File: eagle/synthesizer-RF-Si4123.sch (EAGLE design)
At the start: 46 parts, among them J1 142-0701-851, J2 142-0701-851, J3 142-0701-851, U1 LP38692, U2 SI4123, X1 ECS-TXO-3225

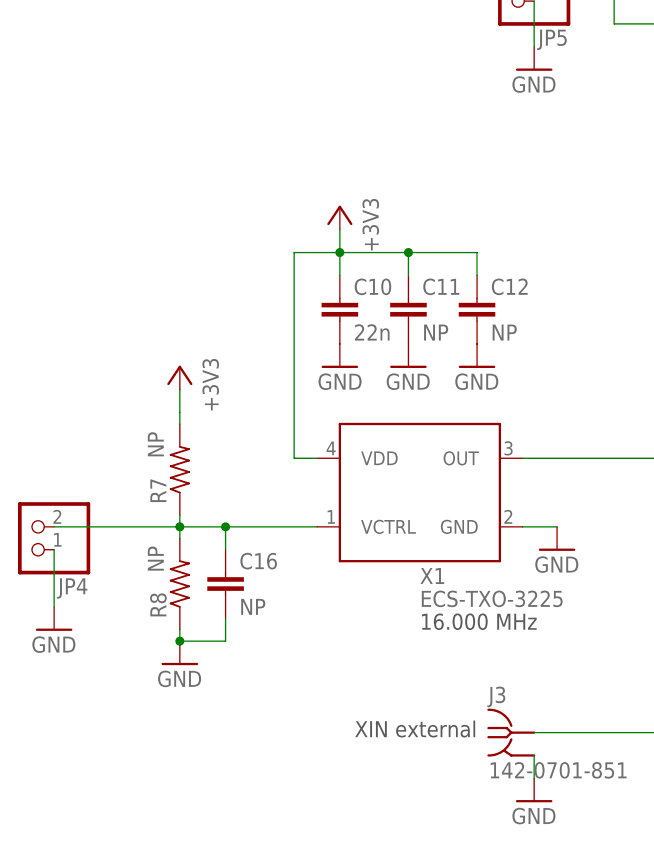
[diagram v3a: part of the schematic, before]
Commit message: Add 0ohm to TCXO, & minor tweaks.
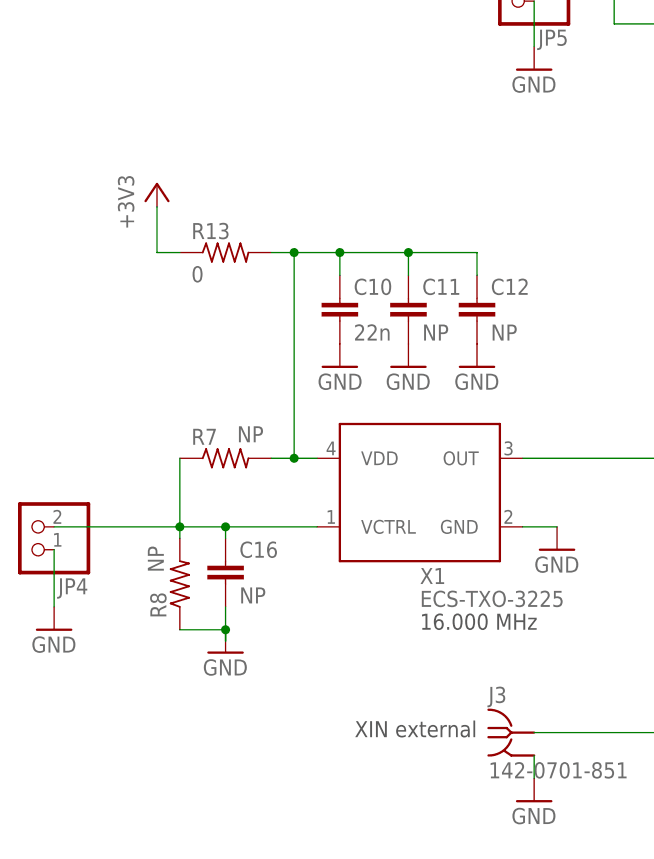
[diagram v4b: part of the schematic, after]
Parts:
- added R13: 0, oresat-rcl:R-US_0805-B-NOSILK
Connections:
- new net N$10: C10.1, C11.1, C12.1, R13.2, R7.2, X1.VDD
- net +3V3: now also R13.1; no longer C10.1, C11.1, C12.1, R7.2, X1.VDD
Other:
- moved on the sheet: C16, R7
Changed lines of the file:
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@@
 <part name="R7" library="oresat-rcl" deviceset="R-US_" device="0603-B-NOSILK" value="NP"/>
 <part name="R8" library="oresat-rcl" deviceset="R-US_" device="0603-B-NOSILK" value="NP"/>
-<part name="+3V1" library="supply1" library_urn="urn:adsk.eagle:library:371" deviceset="+3V3" device=""/>
 <part name="GND10" library="supply1" library_urn="urn:adsk.eagle:library:371" deviceset="GND" device=""/>
 <part name="GND11" library="supply1" library_urn="urn:adsk.eagle:library:371" deviceset="GND" device=""/>
@@
 <part name="L2" library="oresat-rcl" deviceset="L-US" device="0402-C-NOSILK" value="18/2.7n"/>
 <part name="L3" library="oresat-rcl" deviceset="L-US" device="0402-B-NOSILK" value="2n"/>
+<part name="R13" library="oresat-rcl" deviceset="R-US_" device="0805-B-NOSILK" value="0"/>
 </parts>
 <sheets>
@@
 <attribute name="VALUE" x="101.6" y="125.73" size="1.778" layer="96" rot="R90"/>
 </instance>
-<instance part="+3V8" gate="G$1" x="55.88" y="81.28" smashed="yes" rot="MR0">
-<attribute name="VALUE" x="58.42" y="76.2" size="1.778" layer="96" rot="MR90"/>
+<instance part="+3V8" gate="G$1" x="35.56" y="83.82" smashed="yes">
+<attribute name="VALUE" x="33.02" y="78.74" size="1.778" layer="96" rot="R90"/>
 </instance>
 <instance part="JP4" gate="G$1" x="21.59" y="45.72" smashed="yes" rot="R180">
@@
 </instance>
 <instance part="JMP1" gate="G$2" x="106.68" y="50.8" smashed="yes"/>
-<instance part="R7" gate="R" x="38.1" y="52.07" smashed="yes" rot="R90">
-<attribute name="NAME" x="36.6014" y="48.26" size="1.778" layer="95" rot="R90"/>
-<attribute name="VALUE" x="36.322" y="53.34" size="1.778" layer="96" rot="R90"/>
+<instance part="R7" gate="R" x="43.18" y="53.34" smashed="yes">
+<attribute name="NAME" x="39.37" y="54.8386" size="1.778" layer="95"/>
+<attribute name="VALUE" x="44.45" y="55.118" size="1.778" layer="96"/>
 </instance>
 <instance part="R8" gate="R" x="38.1" y="39.37" smashed="yes" rot="R90">
@@
 <attribute name="VALUE" x="36.322" y="40.64" size="1.778" layer="96" rot="R90"/>
 </instance>
-<instance part="+3V1" gate="G$1" x="38.1" y="63.5" smashed="yes" rot="MR0">
-<attribute name="VALUE" x="40.64" y="58.42" size="1.778" layer="96" rot="MR90"/>
-</instance>
-<instance part="GND10" gate="1" x="38.1" y="30.48" smashed="yes">
-<attribute name="VALUE" x="35.56" y="27.94" size="1.778" layer="96"/>
+<instance part="GND10" gate="1" x="43.18" y="31.75" smashed="yes">
+<attribute name="VALUE" x="40.64" y="29.21" size="1.778" layer="96"/>
 </instance>
 <instance part="GND11" gate="1" x="91.44" y="166.37" smashed="yes">
@@
 <attribute name="VALUE" x="186.182" y="66.04" size="1.778" layer="96" rot="R90"/>
 </instance>
-<instance part="C16" gate="CE" x="43.18" y="40.64" smashed="yes">
-<attribute name="NAME" x="44.704" y="41.021" size="1.778" layer="95"/>
-<attribute name="VALUE" x="44.704" y="35.941" size="1.778" layer="96"/>
+<instance part="C16" gate="CE" x="43.18" y="41.91" smashed="yes">
+<attribute name="NAME" x="44.704" y="42.291" size="1.778" layer="95"/>
+<attribute name="VALUE" x="44.704" y="37.211" size="1.778" layer="96"/>
 </instance>
 <instance part="L1" gate="L" x="119.38" y="95.25" smashed="yes" rot="R90">
@@
 <attribute name="NAME" x="185.42" y="102.87" size="1.778" layer="95" rot="R180"/>
 <attribute name="VALUE" x="180.34" y="102.87" size="1.778" layer="96" rot="R180"/>
+</instance>
+<instance part="R13" gate="R" x="43.18" y="76.2" smashed="yes">
+<attribute name="NAME" x="39.37" y="77.6986" size="1.778" layer="95"/>
+<attribute name="VALUE" x="39.37" y="72.898" size="1.778" layer="96"/>
 </instance>
 </instances>
@@
 <pinref part="R8" gate="R" pin="1"/>
 <pinref part="GND10" gate="1" pin="GND"/>
-<wire x1="38.1" y1="34.29" x2="38.1" y2="33.02" width="0.1524" layer="91"/>
+<wire x1="38.1" y1="34.29" x2="43.18" y2="34.29" width="0.1524" layer="91"/>
 <pinref part="C16" gate="CE" pin="2"/>
-<wire x1="38.1" y1="33.02" x2="43.18" y2="33.02" width="0.1524" layer="91"/>
-<wire x1="43.18" y1="33.02" x2="43.18" y2="35.56" width="0.1524" layer="91"/>
-<junction x="38.1" y="33.02"/>
+<wire x1="43.18" y1="34.29" x2="43.18" y2="33.02" width="0.1524" layer="91"/>
+<wire x1="43.18" y1="33.02" x2="43.18" y2="36.83" width="0.1524" layer="91"/>
+<junction x="43.18" y="34.29"/>
 </segment>
 <segment>
@@
 <wire x1="104.14" y1="125.73" x2="104.14" y2="128.27" width="0.1524" layer="91"/>
 <pinref part="+3V7" gate="G$1" pin="+3V3"/>
-</segment>
-<segment>
-<pinref part="C12" gate="CE" pin="1"/>
-<wire x1="71.12" y1="73.66" x2="71.12" y2="76.2" width="0.1524" layer="91"/>
-<pinref part="C11" gate="CE" pin="1"/>
-<wire x1="63.5" y1="73.66" x2="63.5" y2="76.2" width="0.1524" layer="91"/>
-<wire x1="63.5" y1="76.2" x2="71.12" y2="76.2" width="0.1524" layer="91"/>
-<pinref part="C10" gate="CE" pin="1"/>
-<wire x1="63.5" y1="76.2" x2="55.88" y2="76.2" width="0.1524" layer="91"/>
-<wire x1="55.88" y1="76.2" x2="55.88" y2="73.66" width="0.1524" layer="91"/>
-<junction x="63.5" y="76.2"/>
-<junction x="55.88" y="76.2"/>
-<wire x1="55.88" y1="78.74" x2="55.88" y2="76.2" width="0.1524" layer="91"/>
-<pinref part="+3V8" gate="G$1" pin="+3V3"/>
-<pinref part="X1" gate="G$1" pin="VDD"/>
-<wire x1="53.34" y1="53.34" x2="50.8" y2="53.34" width="0.1524" layer="91"/>
-<wire x1="50.8" y1="53.34" x2="50.8" y2="76.2" width="0.1524" layer="91"/>
-<wire x1="50.8" y1="76.2" x2="55.88" y2="76.2" width="0.1524" layer="91"/>
-</segment>
-<segment>
-<pinref part="R7" gate="R" pin="2"/>
-<pinref part="+3V1" gate="G$1" pin="+3V3"/>
-<wire x1="38.1" y1="57.15" x2="38.1" y2="58.42" width="0.1524" layer="91"/>
-<wire x1="38.1" y1="58.42" x2="38.1" y2="60.96" width="0.1524" layer="91"/>
 </segment>
 <segment>
@@
 <wire x1="149.86" y1="185.42" x2="111.76" y2="185.42" width="0.1524" layer="91"/>
 </segment>
+<segment>
+<pinref part="+3V8" gate="G$1" pin="+3V3"/>
+<pinref part="R13" gate="R" pin="1"/>
+<wire x1="35.56" y1="81.28" x2="35.56" y2="76.2" width="0.1524" layer="91"/>
+<wire x1="35.56" y1="76.2" x2="38.1" y2="76.2" width="0.1524" layer="91"/>
+</segment>
 </net>
 <net name="N$19" class="0">
@@
 <wire x1="43.18" y1="45.72" x2="38.1" y2="45.72" width="0.1524" layer="91"/>
 <wire x1="38.1" y1="45.72" x2="24.13" y2="45.72" width="0.1524" layer="91"/>
-<wire x1="38.1" y1="46.99" x2="38.1" y2="45.72" width="0.1524" layer="91"/>
+<wire x1="38.1" y1="53.34" x2="38.1" y2="45.72" width="0.1524" layer="91"/>
 <junction x="38.1" y="45.72"/>
 <pinref part="R8" gate="R" pin="2"/>
@@
 <junction x="43.18" y="45.72"/>
 <pinref part="C16" gate="CE" pin="1"/>
-<wire x1="43.18" y1="43.18" x2="43.18" y2="45.72" width="0.1524" layer="91"/>
+<wire x1="43.18" y1="44.45" x2="43.18" y2="45.72" width="0.1524" layer="91"/>
 </segment>
 </net>
@@
 </segment>
 </net>
+<net name="N$10" class="0">
+<segment>
+<pinref part="C12" gate="CE" pin="1"/>
+<wire x1="71.12" y1="73.66" x2="71.12" y2="76.2" width="0.1524" layer="91"/>
+<pinref part="C11" gate="CE" pin="1"/>
+<wire x1="63.5" y1="73.66" x2="63.5" y2="76.2" width="0.1524" layer="91"/>
+<wire x1="63.5" y1="76.2" x2="71.12" y2="76.2" width="0.1524" layer="91"/>
+<pinref part="C10" gate="CE" pin="1"/>
+<wire x1="63.5" y1="76.2" x2="55.88" y2="76.2" width="0.1524" layer="91"/>
+<wire x1="55.88" y1="76.2" x2="55.88" y2="73.66" width="0.1524" layer="91"/>
+<junction x="63.5" y="76.2"/>
+<junction x="55.88" y="76.2"/>
+<pinref part="X1" gate="G$1" pin="VDD"/>
+<wire x1="53.34" y1="53.34" x2="50.8" y2="53.34" width="0.1524" layer="91"/>
+<wire x1="50.8" y1="53.34" x2="50.8" y2="76.2" width="0.1524" layer="91"/>
+<wire x1="50.8" y1="76.2" x2="55.88" y2="76.2" width="0.1524" layer="91"/>
+<pinref part="R13" gate="R" pin="2"/>
+<wire x1="48.26" y1="76.2" x2="50.8" y2="76.2" width="0.1524" layer="91"/>
+<junction x="50.8" y="76.2"/>
+<pinref part="R7" gate="R" pin="2"/>
+<wire x1="48.26" y1="53.34" x2="50.8" y2="53.34" width="0.1524" layer="91"/>
+<junction x="50.8" y="53.34"/>
+</segment>
+</net>

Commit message: Change resistor sizes. Add tstop to L1/2 traces.
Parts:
- R1, R13, R2: device oresat-rcl:R-US_0805-B-NOSILK -> oresat-rcl:R-US_0603-B-NOSILK
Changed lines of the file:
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@@
 <part name="R6" library="oresat-rcl" deviceset="R-US_" device="0402-B-NOSILK" value="47k"/>
 <part name="C7" library="oresat-rcl" deviceset="C-EU" device="0603-B-NOSILK" value="22n"/>
-<part name="R2" library="oresat-rcl" deviceset="R-US_" device="0805-B-NOSILK" value="0"/>
+<part name="R2" library="oresat-rcl" deviceset="R-US_" device="0603-B-NOSILK" value="0"/>
 <part name="L4" library="oresat-rcl" deviceset="L-US" device="0402-B-NOSILK" value="47n"/>
 <part name="C8" library="oresat-rcl" deviceset="C-EU" device="0402-B-NOSILK" value="560p"/>
@@
 <part name="C11" library="oresat-rcl" deviceset="C-EU" device="0603-B-NOSILK" value="NP"/>
 <part name="GND111" library="supply1" library_urn="urn:adsk.eagle:library:371" deviceset="GND" device=""/>
-<part name="R1" library="oresat-rcl" deviceset="R-US_" device="0805-B-NOSILK" value="0"/>
+<part name="R1" library="oresat-rcl" deviceset="R-US_" device="0603-B-NOSILK" value="0"/>
 <part name="+3V5" library="supply1" library_urn="urn:adsk.eagle:library:371" deviceset="+3V3" device=""/>
 <part name="+3V6" library="supply1" library_urn="urn:adsk.eagle:library:371" deviceset="+3V3" device=""/>
@@
 <part name="L2" library="oresat-rcl" deviceset="L-US" device="0402-C-NOSILK" value="18/2.7n"/>
 <part name="L3" library="oresat-rcl" deviceset="L-US" device="0402-B-NOSILK" value="2n"/>
-<part name="R13" library="oresat-rcl" deviceset="R-US_" device="0805-B-NOSILK" value="0"/>
+<part name="R13" library="oresat-rcl" deviceset="R-US_" device="0603-B-NOSILK" value="0"/>
 </parts>
 <sheets>

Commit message: Added stitching
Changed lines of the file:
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@@
 </class>
 <class number="2" name="RF2" width="0" drill="0">
-<clearance class="2" value="0.1778"/>
+<clearance class="2" value="0.2032"/>
 </class>
 </classes>
@@
 <attribute name="VALUE" x="36.322" y="40.64" size="1.778" layer="96" rot="R90"/>
 </instance>
-<instance part="GND10" gate="1" x="43.18" y="31.75" smashed="yes">
-<attribute name="VALUE" x="40.64" y="29.21" size="1.778" layer="96"/>
+<instance part="GND10" gate="1" x="38.1" y="30.48" smashed="yes">
+<attribute name="VALUE" x="35.56" y="27.94" size="1.778" layer="96"/>
 </instance>
 <instance part="GND11" gate="1" x="91.44" y="166.37" smashed="yes">
@@
 <pinref part="R8" gate="R" pin="1"/>
 <pinref part="GND10" gate="1" pin="GND"/>
-<wire x1="38.1" y1="34.29" x2="43.18" y2="34.29" width="0.1524" layer="91"/>
+<wire x1="38.1" y1="34.29" x2="38.1" y2="33.02" width="0.1524" layer="91"/>
 <pinref part="C16" gate="CE" pin="2"/>
-<wire x1="43.18" y1="34.29" x2="43.18" y2="33.02" width="0.1524" layer="91"/>
+<wire x1="38.1" y1="33.02" x2="43.18" y2="33.02" width="0.1524" layer="91"/>
 <wire x1="43.18" y1="33.02" x2="43.18" y2="36.83" width="0.1524" layer="91"/>
-<junction x="43.18" y="34.29"/>
+<junction x="38.1" y="33.02"/>
 </segment>
 <segment>
@@
 </sheet>
 </sheets>
+<errors>
+</errors>
 </schematic>
 </drawing>

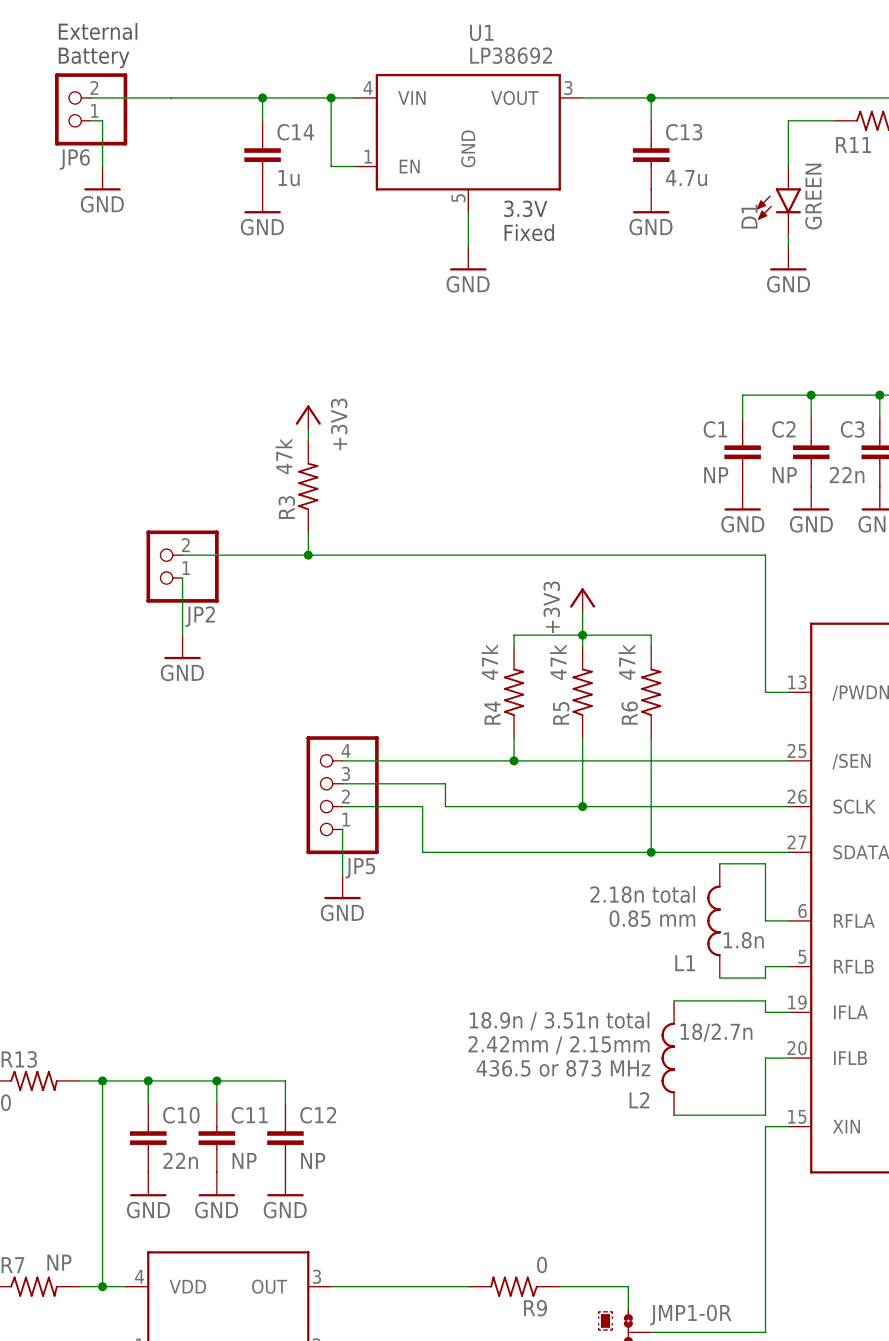
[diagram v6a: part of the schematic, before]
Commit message: Update cap values
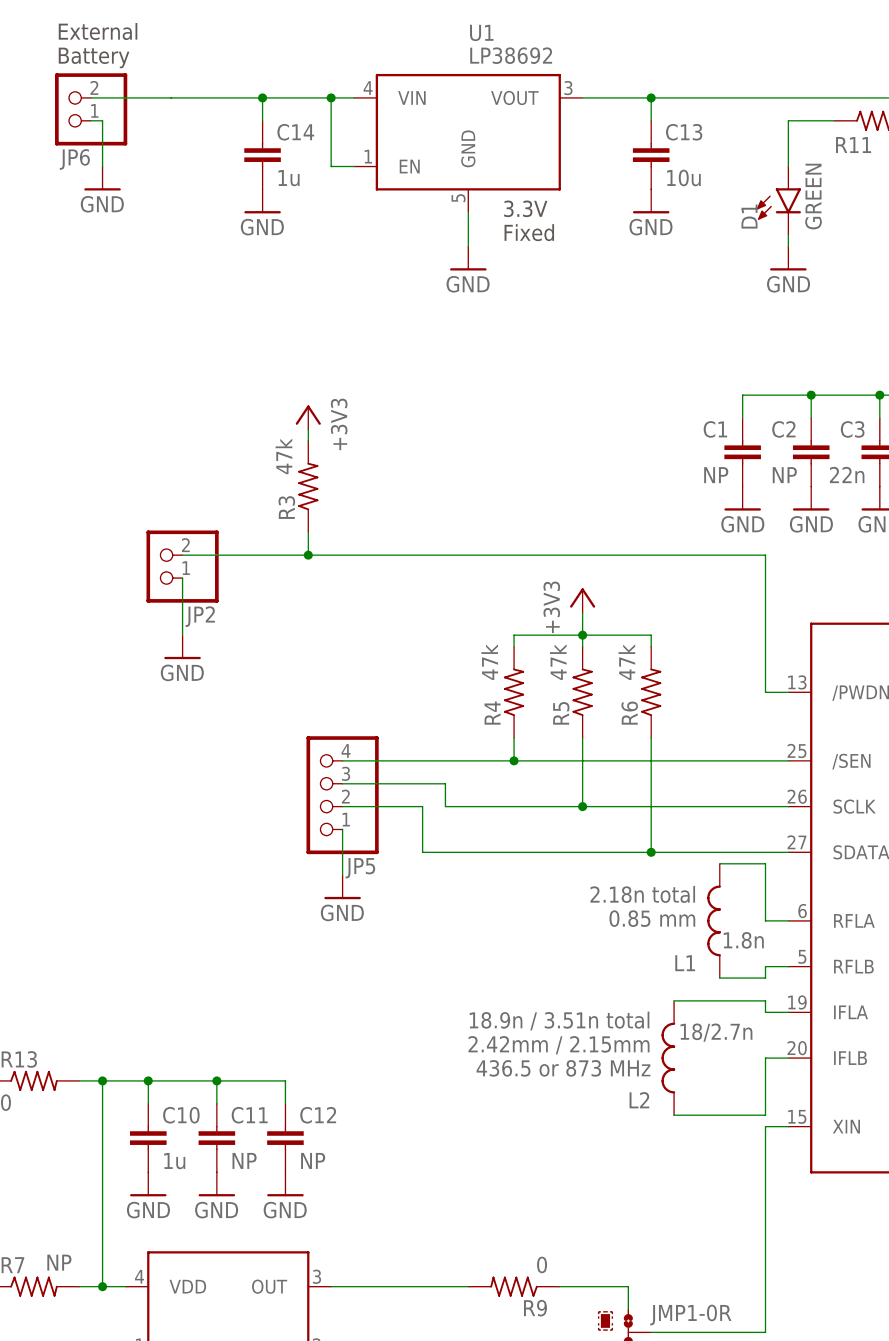
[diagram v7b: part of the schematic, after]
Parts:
- C10: value 22n -> 1u
- C13: value 4.7u -> 10u
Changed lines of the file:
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@@
 <part name="R9" library="oresat-rcl" deviceset="R-US_" device="0402-B-NOSILK" value="0"/>
 <part name="R10" library="oresat-rcl" deviceset="R-US_" device="0402-B-NOSILK" value="0"/>
-<part name="C10" library="oresat-rcl" deviceset="C-EU" device="0603-B-NOSILK" value="22n"/>
+<part name="C10" library="oresat-rcl" deviceset="C-EU" device="0603-B-NOSILK" value="1u"/>
 <part name="GND13" library="supply1" library_urn="urn:adsk.eagle:library:371" deviceset="GND" device=""/>
 <part name="X1" library="X-ECS-TXO-TCXO" deviceset="ECS-TXO-3225" device=""/>
@@
 <part name="GND11" library="supply1" library_urn="urn:adsk.eagle:library:371" deviceset="GND" device=""/>
 <part name="JP6" library="pinhead" library_urn="urn:adsk.eagle:library:325" deviceset="PINHD-1X2" device="" package3d_urn="urn:adsk.eagle:package:22435/2"/>
-<part name="C13" library="oresat-rcl" deviceset="C-EU" device="0805-B-NOSILK" value="4.7u"/>
+<part name="C13" library="oresat-rcl" deviceset="C-EU" device="0805-B-NOSILK" value="10u"/>
 <part name="C14" library="oresat-rcl" deviceset="C-EU" device="0603-B-NOSILK" value="1u"/>
 <part name="GND87" library="supply1" library_urn="urn:adsk.eagle:library:371" deviceset="GND" device=""/>

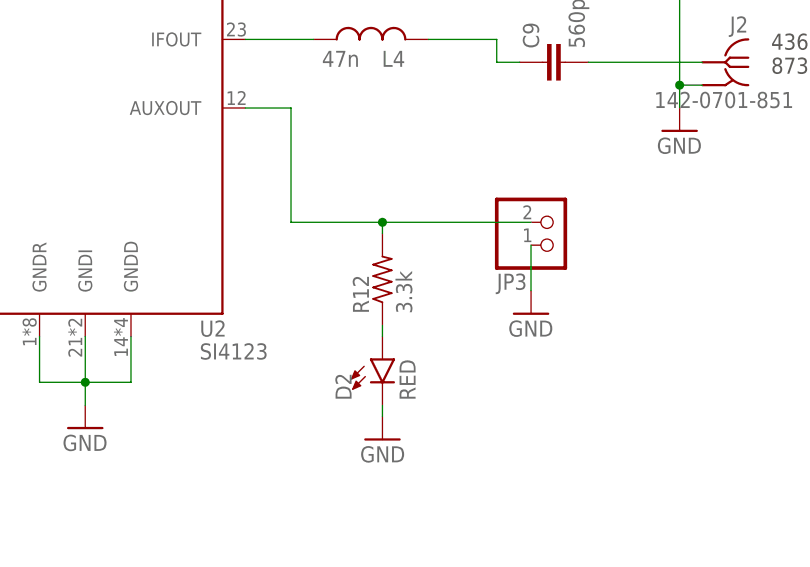
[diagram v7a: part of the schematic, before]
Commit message: Update LED resistor
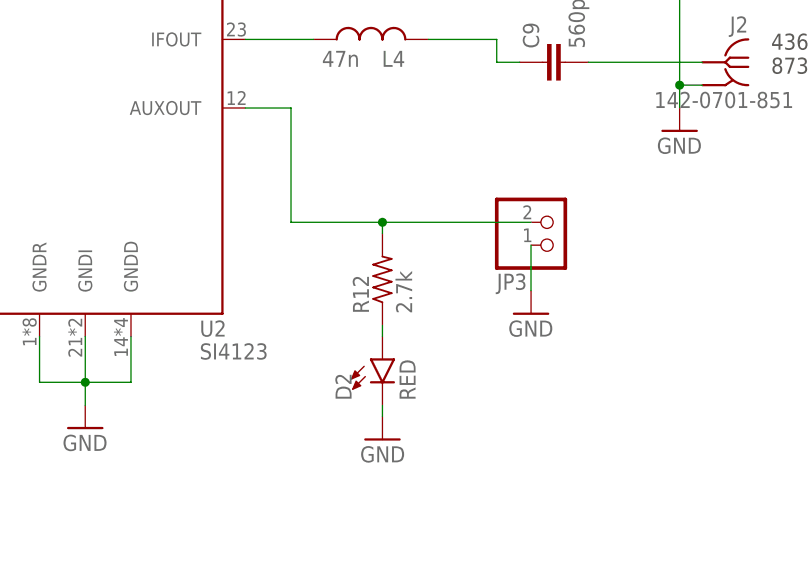
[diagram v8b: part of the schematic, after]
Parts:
- R12: value 3.3k -> 2.7k
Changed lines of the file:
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@@
 </part>
 <part name="GND14" library="supply1" deviceset="GND" device=""/>
-<part name="R12" library="oresat-rcl" deviceset="R-US_" device="0603-B-NOSILK" value="3.3k"/>
+<part name="R12" library="oresat-rcl" deviceset="R-US_" device="0603-B-NOSILK" value="2.7k"/>
 <part name="C16" library="oresat-rcl" deviceset="C-EU" device="0603-B-NOSILK" value="NP"/>
 <part name="L1" library="oresat-rcl" deviceset="L-US" device="0402-C-NOSILK" value="1.8n"/>
